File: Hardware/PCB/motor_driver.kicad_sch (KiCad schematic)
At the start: 6 parts, among them J6 Brushed Motor Coil, J8 Brushless DC Motor, U3 DRV8871DDA

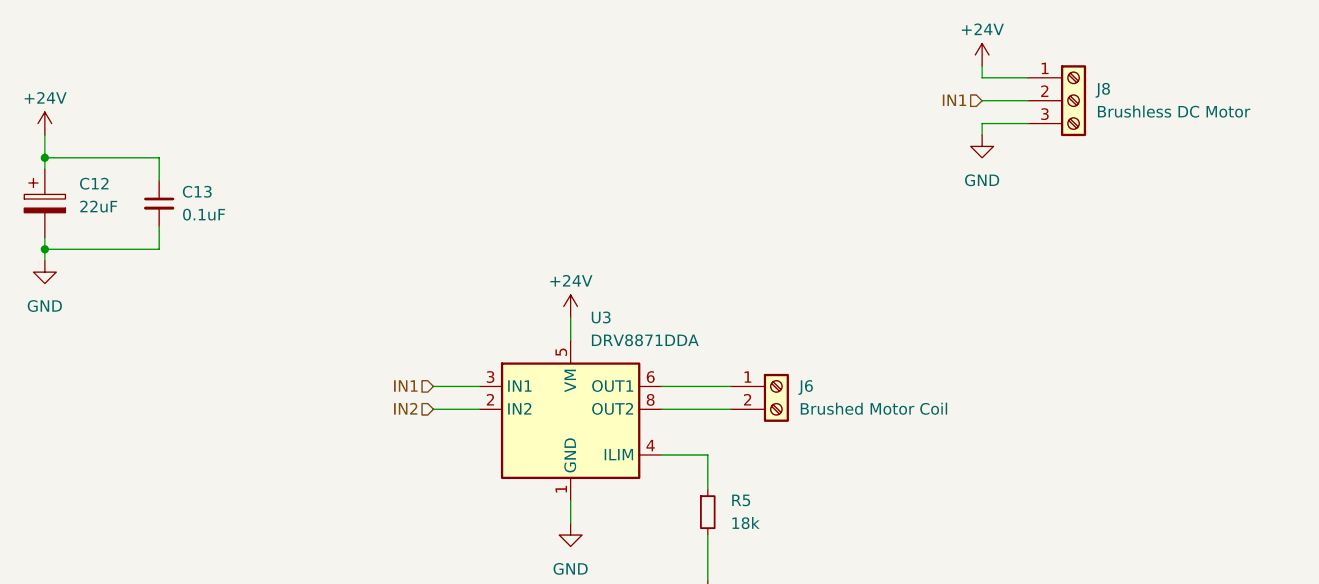
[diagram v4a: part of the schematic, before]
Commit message: overall design is pretty much done, starting layout and routing now
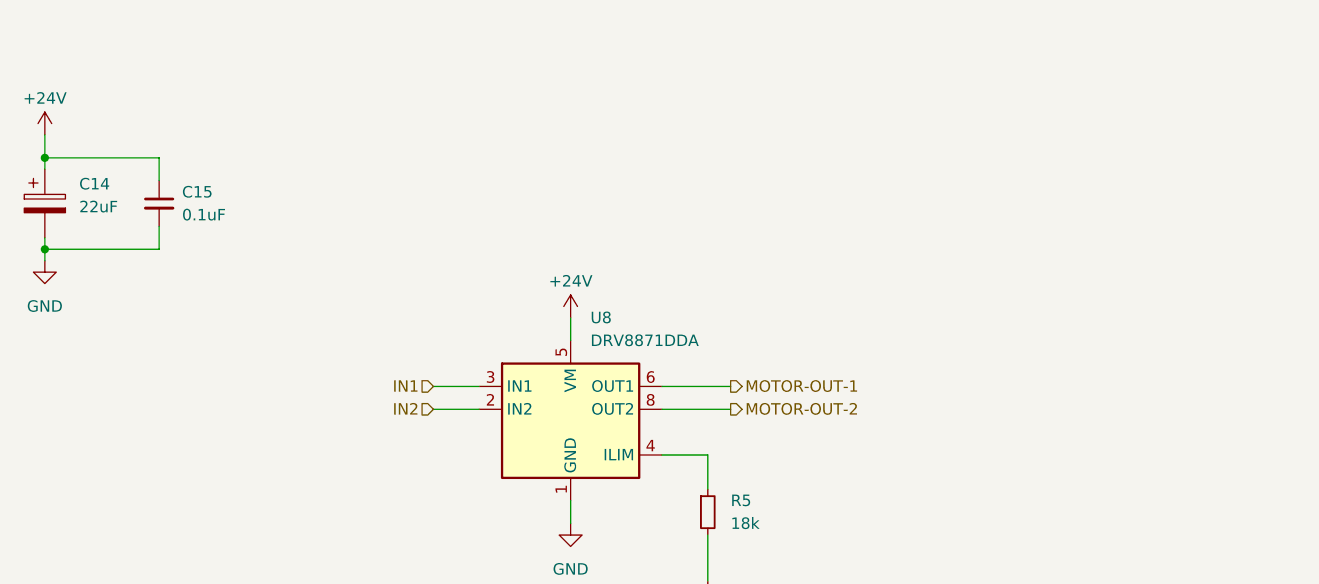
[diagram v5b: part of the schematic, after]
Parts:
- removed J6: Brushed Motor Coil, Vendor_Footprints:CONN2_1-2834011-2_TEC, symbol Connector:Screw_Terminal_01x02
- removed J8: Brushless DC Motor, Vendor_Footprints:CONN_1-2834011-3_TEC, symbol Connector:Screw_Terminal_01x03
- U8: renamed from U3; DigiKey Link (none) -> https://www.digikey.com/en/products/detail/texas-instrument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; MPN (none) -> DRV8871DDAR; Manufacturer (none) -> Texas Instruments
- renumbered C12 to C14, C13 to C15
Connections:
- net MOTOR-OUT-1: now reaches U8.6 (OUT1)
- net MOTOR-OUT-2: now reaches U8.8 (OUT2)

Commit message: kinda pricey, I should try to make a smaller version using LCSC parts for cheaper solution
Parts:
- C14: LCSC (none) -> C2162918
- C15: LCSC (none) -> C73745
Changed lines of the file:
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@@
+			)
+		)
+		(property "LCSC" "C2162918"
+			(at 38.1 44.45 0)
+			(effects
+				(font
+					(size 1.27 1.27)
+				)
 			)
 		)
@@
 			)
 		)
+		(property "LCSC" "C73745"
+			(at 50.8 44.45 0)
+			(effects
+				(font
+					(size 1.27 1.27)
+				)
+			)
+		)
 		(pin "1"
 		)
@@
 			)
 		)
+		(property "LCSC" ""
+			(at 111.76 78.74 0)
+			(effects
+				(font
+					(size 1.27 1.27)
+				)
+			)
+		)
 		(pin "1"
 		)
@@
 			)
 		)
+		(property "LCSC" ""
+			(at 96.52 67.31 0)
+			(effects
+				(font
+					(size 1.27 1.27)
+				)
+			)
+		)

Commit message: done with this, placed order
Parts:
- added J1: Pump Motor, Vendor_Footprints:CONN_WJ15EDGRC-3.81-2P, symbol Connector:Screw_Terminal_01x02
- C14: LCSC C2162918 -> C29144; MPN UUX2A220MNL6GS -> RVT2A220M0810; Manufacturer Nichicon -> Honor Elec
- C15: value 0.1uF -> 100nF; footprint Capacitor_SMD:C_1206_3216Metric_Pad1.33x1.80mm_HandSolder -> Capacitor_SMD:C_0603_1608Metric_Pad1.08x0.95mm_HandSolder; LCSC C73745 -> C14663; MPN CL31B104KEHSFNE -> CC0603KRX7R9BB104; Manufacturer Samsung Electro-Mechanics -> YAGEO
- R5: footprint Resistor_SMD:R_1206_3216Metric_Pad1.30x1.75mm_HandSolder -> Resistor_SMD:R_0805_2012Metric_Pad1.20x1.40mm_HandSolder; LCSC (none) -> C2907231; MPN CR1206-FX-1802ELF -> FRC0805F1802TS; Manufacturer Bourns Inc. -> FOJAN
- U8: LCSC (none) -> C75864
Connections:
- net MOTOR-OUT-1: no longer names the net of U8.6 (OUT1)
- net MOTOR-OUT-1: now also J1.2 (Pin_2)
- net MOTOR-OUT-2: no longer names the net of U8.8 (OUT2)
- net MOTOR-OUT-2: now also J1.1 (Pin_1)
